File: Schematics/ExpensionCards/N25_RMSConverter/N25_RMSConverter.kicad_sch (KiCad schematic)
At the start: 72 parts

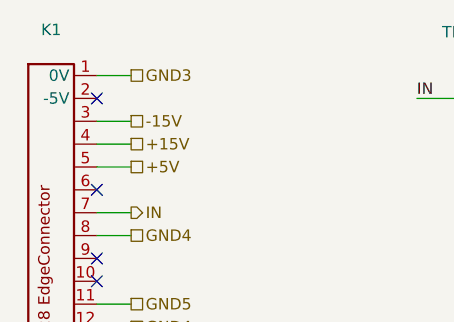
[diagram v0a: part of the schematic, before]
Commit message: Reworked N20/N21
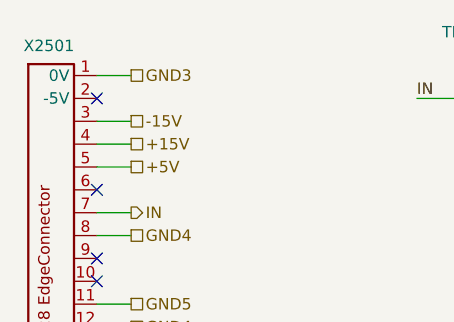
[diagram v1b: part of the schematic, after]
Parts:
- R2504, R2510, R2514, R2517: footprint PM2528:Potentiometer horizontal ceramic -> PM2528:Trimmer vertical
- TP2501, TP2502, TP2503, TP2504, TP2505, TP2506, TP2507: footprint Connector_PinHeader_1.00mm:PinHeader_1x01_P1.00mm_Vertical -> Connector_Pin:Pin_D0.9mm_L10.0mm_W2.4mm_FlatFork
- renumbered JP4 to JP2501, JP3 to JP2502, JP2 to JP2503, JP1 to JP2504, K1 to X2501
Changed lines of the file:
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@@
 		(on_board yes)
 		(dnp no)
-		(property "Reference" "JP1"
+		(property "Reference" "JP2504"
 			(at 287.02 81.28 0)
 			(effects
@@
 			(project ""
 				(path "/210e0b9d-97f4-4fba-8363-ab76276771d7"
-					(reference "JP1")
+					(reference "JP2504")
 					(unit 1)
 				)
@@
 		(on_board yes)
 		(dnp no)
-		(property "Reference" "JP3"
+		(property "Reference" "JP2502"
 			(at 287.02 96.52 0)
 			(effects
@@
 			(project "N25_RMSConverter"
 				(path "/210e0b9d-97f4-4fba-8363-ab76276771d7"
-					(reference "JP3")
+					(reference "JP2502")
 					(unit 1)
 				)
@@
 		(on_board yes)
 		(dnp no)
-		(fields_autoplaced yes)
-		(property "Reference" "K1"
-			(at 21.59 15.24 0)
+		(property "Reference" "X2501"
+			(at 21.336 17.018 0)
 			(effects
 				(font
@@
 					(size 1.27 1.27)
 				)
+				(hide yes)
 			)
 		)
@@
 			(project ""
 				(path "/210e0b9d-97f4-4fba-8363-ab76276771d7"
-					(reference "K1")
+					(reference "X2501")
 					(unit 1)
 				)
@@
 			)
 		)
-		(property "Footprint" "Connector_PinHeader_1.00mm:PinHeader_1x01_P1.00mm_Vertical"
+		(property "Footprint" "Connector_Pin:Pin_D0.9mm_L10.0mm_W2.4mm_FlatFork"
 			(at 369.57 100.33 0)
 			(effects
@@
 			)
 		)
-		(property "Footprint" "Connector_PinHeader_1.00mm:PinHeader_1x01_P1.00mm_Vertical"
+		(property "Footprint" "Connector_Pin:Pin_D0.9mm_L10.0mm_W2.4mm_FlatFork"
 			(at 130.81 60.96 0)
 			(effects
@@
 			)
 		)
-		(property "Footprint" "PM2528:Potentiometer horizontal ceramic"
+		(property "Footprint" "PM2528:Trimmer vertical"
 			(at 173.99 69.85 0)
 			(effects
@@
 			)
 		)
-		(property "Footprint" "Connector_PinHeader_1.00mm:PinHeader_1x01_P1.00mm_Vertical"
+		(property "Footprint" "Connector_Pin:Pin_D0.9mm_L10.0mm_W2.4mm_FlatFork"
 			(at 233.68 30.48 0)
 			(effects
@@
 			)
 		)
-		(property "Footprint" "PM2528:Potentiometer horizontal ceramic"
+		(property "Footprint" "PM2528:Trimmer vertical"
 			(at 72.39 99.06 0)
 			(effects
@@
 		(on_board yes)
 		(dnp no)
-		(property "Reference" "JP2"
+		(property "Reference" "JP2503"
 			(at 287.02 88.9 0)
 			(effects
@@
 			(project "N25_RMSConverter"
 				(path "/210e0b9d-97f4-4fba-8363-ab76276771d7"
-					(reference "JP2")
+					(reference "JP2503")
 					(unit 1)
 				)
@@
 			)
 		)
-		(property "Footprint" "Connector_PinHeader_1.00mm:PinHeader_1x01_P1.00mm_Vertical"
+		(property "Footprint" "Connector_Pin:Pin_D0.9mm_L10.0mm_W2.4mm_FlatFork"
 			(at 73.66 22.86 0)
 			(effects
@@
 			)
 		)
-		(property "Footprint" "PM2528:Potentiometer horizontal ceramic"
+		(property "Footprint" "PM2528:Trimmer vertical"
 			(at 91.44 55.88 0)
 			(effects
@@
 			)
 		)
-		(property "Footprint" "Connector_PinHeader_1.00mm:PinHeader_1x01_P1.00mm_Vertical"
+		(property "Footprint" "Connector_Pin:Pin_D0.9mm_L10.0mm_W2.4mm_FlatFork"
 			(at 285.75 69.85 0)
 			(effects
@@
 				)
 				(justify left)
+				(hide yes)
 			)
 		)
-		(property "Footprint" "Connector_PinHeader_1.00mm:PinHeader_1x01_P1.00mm_Vertical"
+		(property "Footprint" "Connector_Pin:Pin_D0.9mm_L10.0mm_W2.4mm_FlatFork"
 			(at 92.71 82.55 0)
 			(effects
@@
 			)
 		)
-		(property "Footprint" "Connector_PinHeader_1.00mm:PinHeader_1x01_P1.00mm_Vertical"
+		(property "Footprint" "Connector_Pin:Pin_D0.9mm_L10.0mm_W2.4mm_FlatFork"
 			(at 378.46 205.74 0)
 			(effects
@@
 			)
 		)
-		(property "Footprint" "PM2528:Potentiometer horizontal ceramic"
+		(property "Footprint" "PM2528:Trimmer vertical"
 			(at 293.37 144.78 0)
 			(effects
@@
 		(on_board yes)
 		(dnp no)
-		(property "Reference" "JP4"
+		(property "Reference" "JP2501"
 			(at 287.02 104.14 0)
 			(effects
@@
 			(project "N25_RMSConverter"
 				(path "/210e0b9d-97f4-4fba-8363-ab76276771d7"
-					(reference "JP4")
+					(reference "JP2501")
 					(unit 1)
 				)
